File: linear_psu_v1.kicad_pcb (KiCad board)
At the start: 2 copper layers, 77 x 26.2 mm, 24 parts, among them P1 PowerInput, P2 PowerInput, P3 GND_TESTPOINT, P4 V_IN_TESTPOINT, P5 G +, P6 G +, P7 V_OUT_TESTPOINT, U1 LM78xx

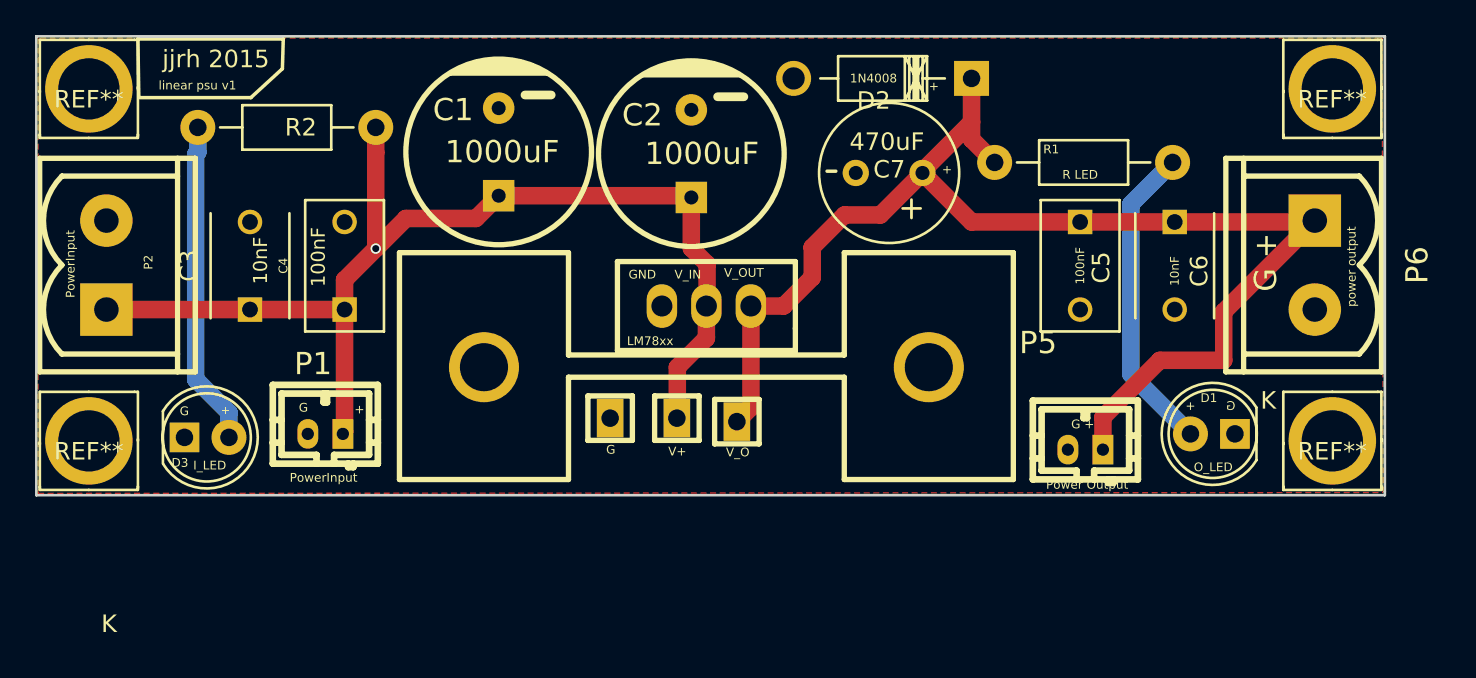
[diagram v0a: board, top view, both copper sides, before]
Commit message: fixed bad footprint, rerouted board
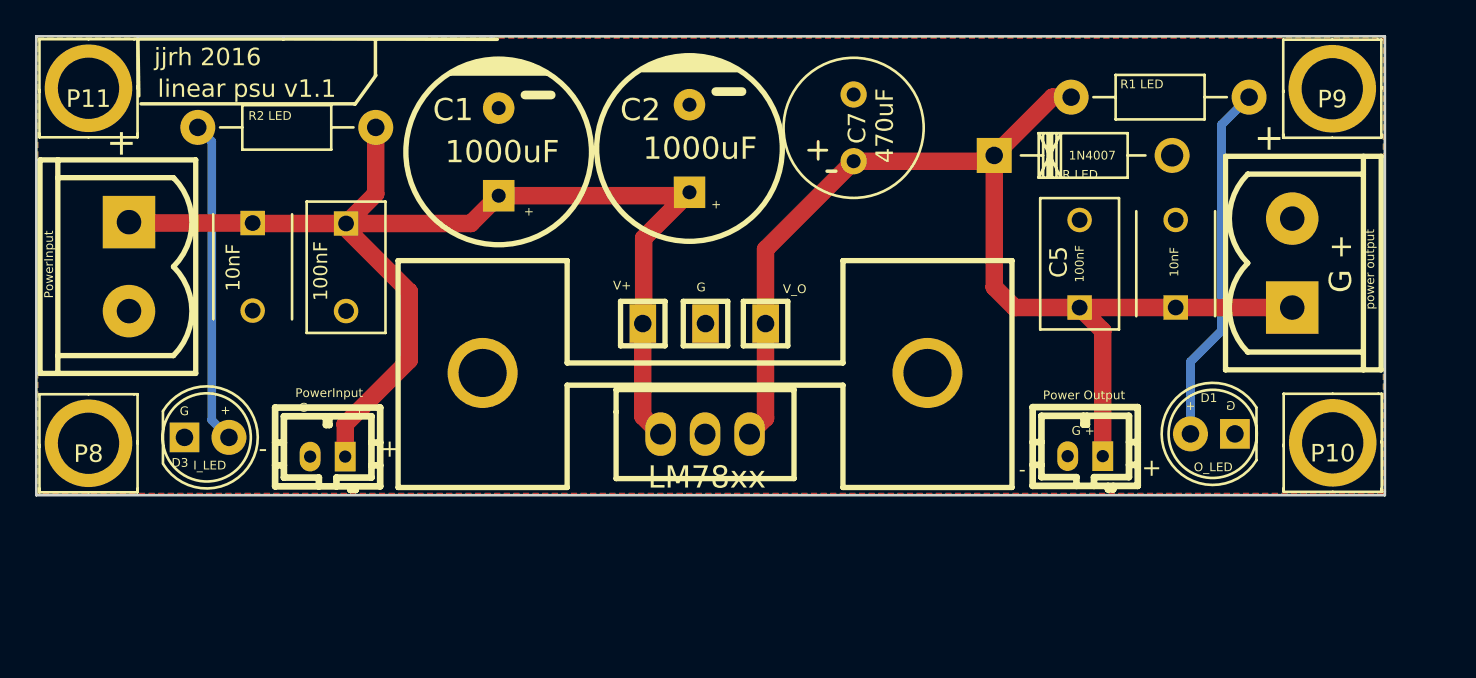
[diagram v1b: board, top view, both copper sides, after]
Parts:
- removed REF** (x4): 3.5mmM3, mechanical:3.5mm_m3
- added P10: MOUNTING_HOLE, mechanical:3.5mm_m3, F.Cu at (184.0, 67.3)
- added P11: MOUNTING_HOLE, mechanical:3.5mm_m3, F.Cu at (113.0, 47.1)
- added P8: MOUNTING_HOLE, mechanical:3.5mm_m3, F.Cu at (113.0, 67.3)
- added P9: MOUNTING_HOLE, mechanical:3.5mm_m3, F.Cu at (184.0, 47.1)
- D2: value 1N4008 -> 1N4007
- R1 LED: renamed from R1
- R2 LED: renamed from R2
- U1: footprint w_to:to220_std_14cw -> lm7805:to220_std_14cw
- moved P3 7.67 mm to (148.2, 60.4)
- moved U1 7.31 mm to (148.2, 66.7), turned to 0 degrees
- moved P7 5.83 mm to (151.6, 60.4)
- moved R1 LED 5.74 mm to (174.2, 47.5)
- moved P4 5.74 mm to (144.6, 60.4)
- moved C3 4.94 mm to (122.4, 54.7), turned to 270 degrees
- moved C4 4.91 mm to (127.7, 54.7), turned to 270 degrees
- moved C5 4.89 mm to (169.6, 59.5), turned to 90 degrees
- moved C6 4.88 mm to (175.1, 59.5), turned to 90 degrees
- moved D2 4.59 mm to (164.7, 50.8), turned to 0 degrees
- moved C7 3.99 mm to (156.7, 51.1), turned to 90 degrees
- moved P1 1.30 mm to (126.6, 68.0)
- moved P2 1.29 mm to (115.3, 57.1), turned to 270 degrees
- moved P6 1.29 mm to (181.7, 56.9), turned to 90 degrees
- moved P5 0.37 mm to (169.9, 68.0)
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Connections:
- U1 pad 1: GNDPWR -> /V+
- U1 pad 2: /V+ -> GNDPWR
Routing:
- net /REG_+5V: track 74.3 -> 66.0 mm
- net /V+: track 65.2 -> 70.6 mm, vias 1 -> 0
- net Net-(D1-Pad2): track 18.1 -> 20.6 mm
- added copper zone on B.Cu, net GNDPWR
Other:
- board text added: "-"
- board text added: "jjrh 2016"
- board text added: "linear psu v1.1"
- board text removed: "GND"
- board text removed: "V_IN"
- board text removed: "V_OUT"
- board text removed: "jjrh 2015"
- board text removed: "linear psu v1"
